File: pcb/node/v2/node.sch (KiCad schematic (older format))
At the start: 99 parts, among them IC1 Ra-01, J1 Sensor1, J10 Conn_02x03_Odd_Even, J11 USB_A, J12 USART2, J13 USART3, J14 LED_EXT, J15 EXT2, J16 USB_OTG, J2 Sensor2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

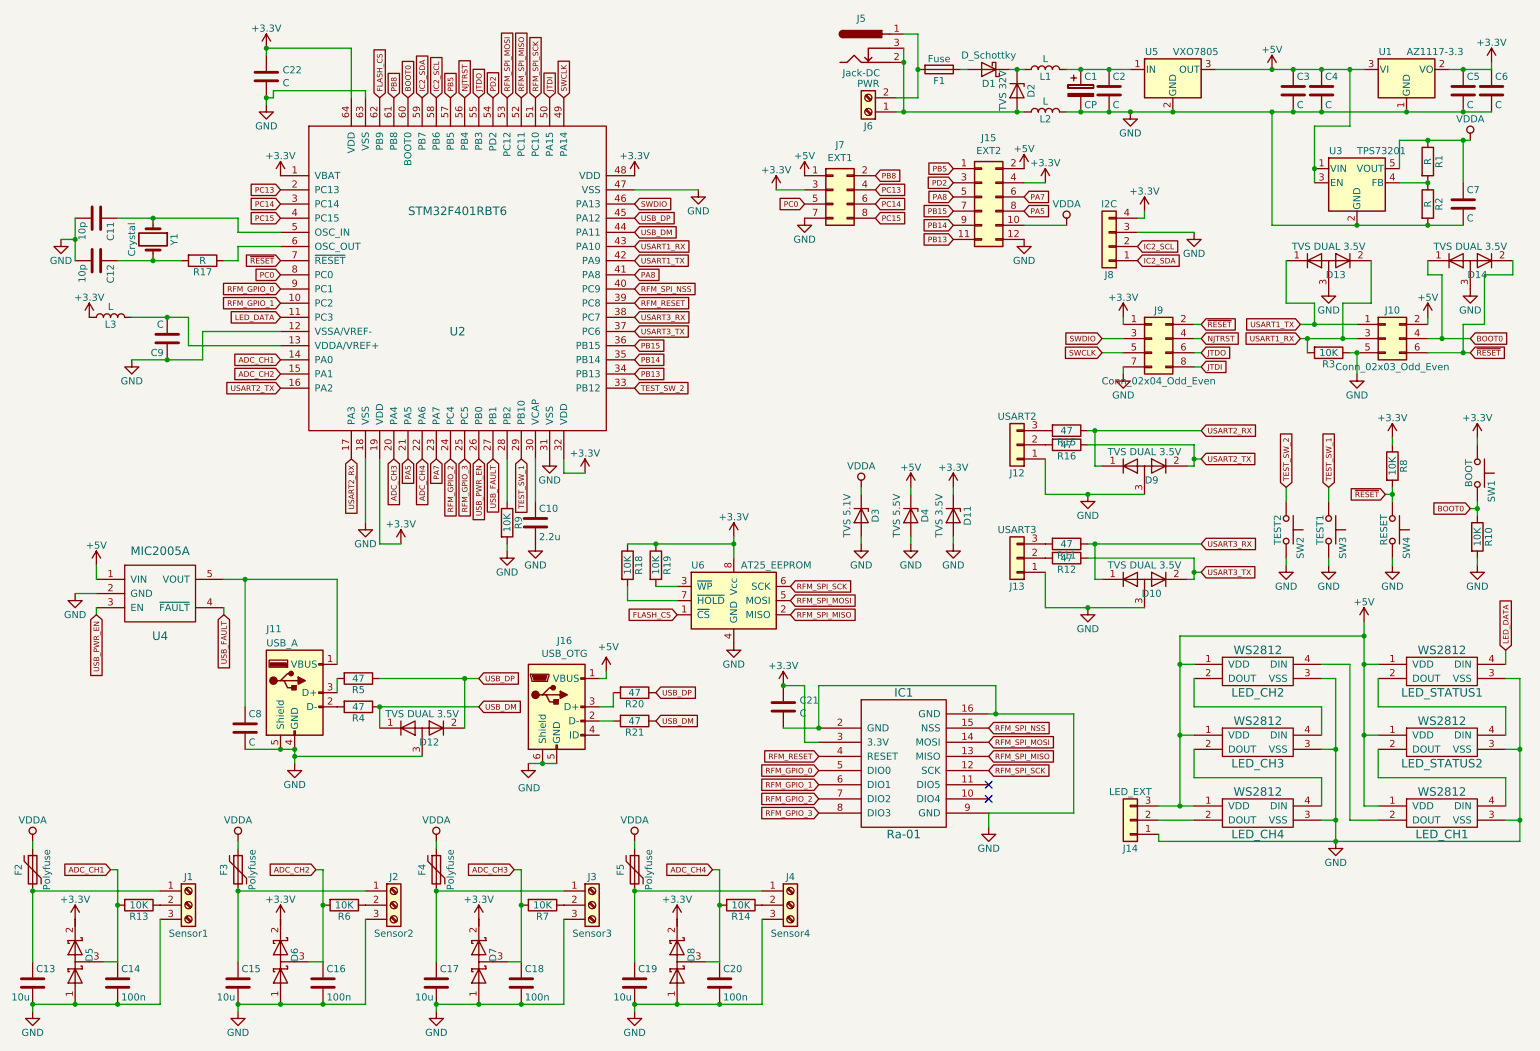
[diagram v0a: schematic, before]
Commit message: Added missing part values
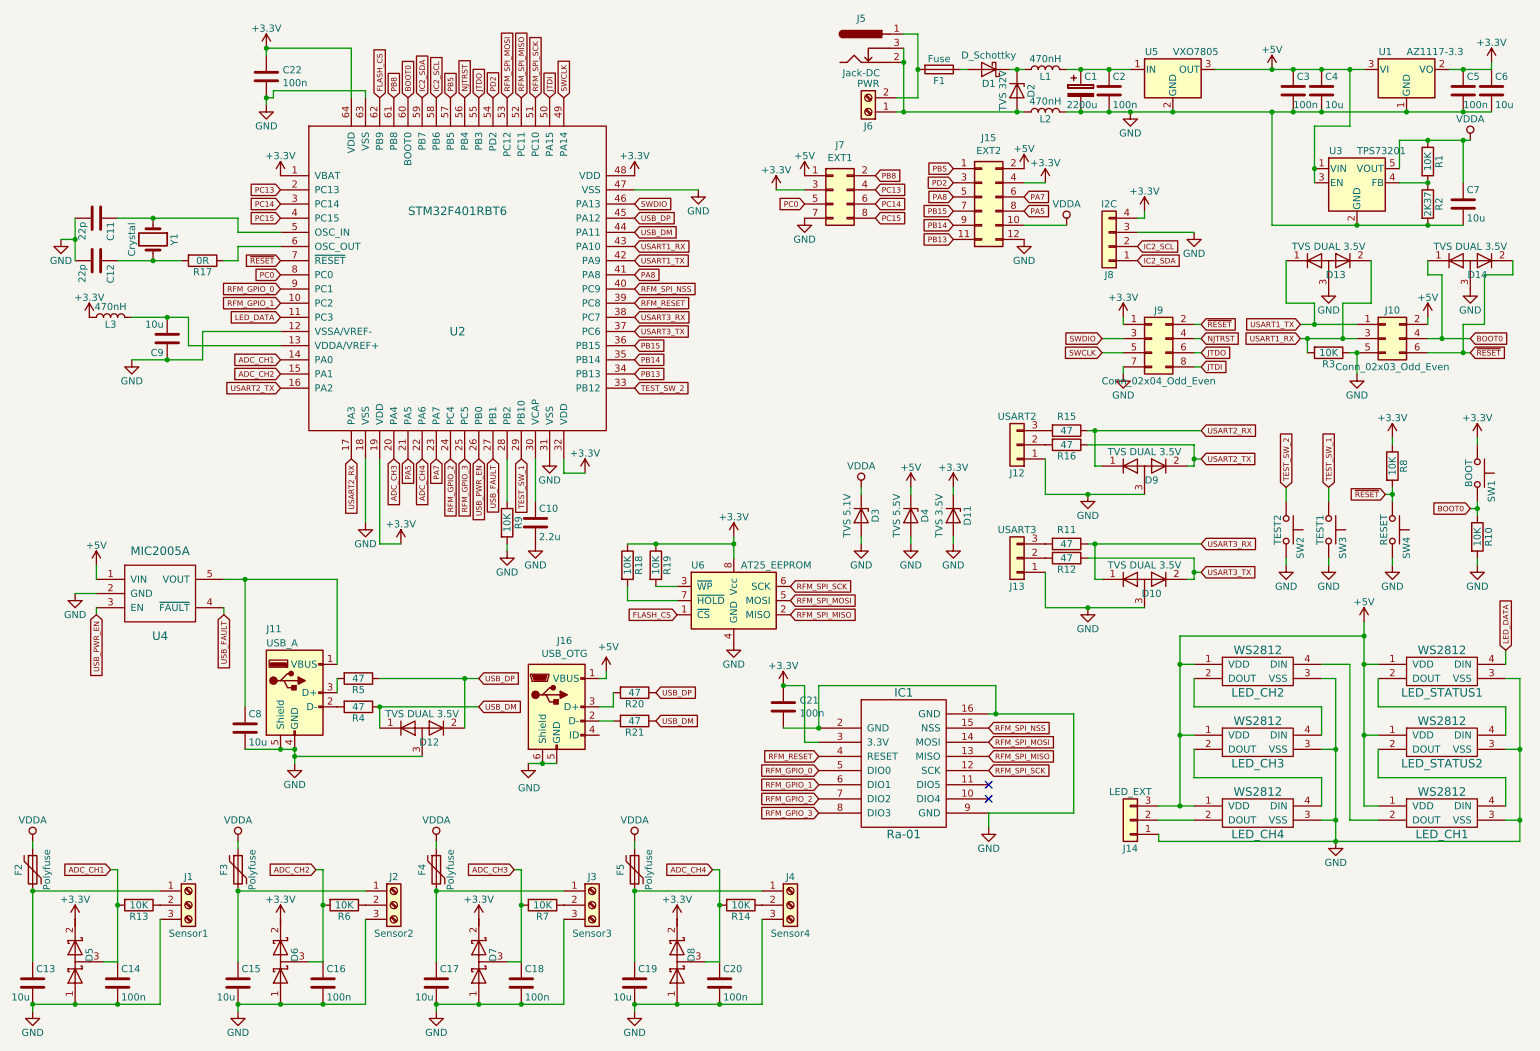
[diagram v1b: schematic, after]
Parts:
- C1: value CP -> 2200u
- C11, C12: value 10p -> 22p
- C2, C21, C22, C3, C5: value C -> 100n
- C4, C6, C7, C8, C9: value C -> 10u
- L1, L2, L3: value L -> 470nH
- R1: value R -> 10K
- R17: value R -> 0R
- R2: value R -> 2K37
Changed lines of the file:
@@
 P 1100 1950
 F 0 "C11" H 1125 2050 50  0000 L CNN
-F 1 "10p" H 1125 1850 50  0000 L CNN
+F 1 "22p" H 1125 1850 50  0000 L CNN
 F 2 "Capacitors_SMD:C_0805" H 1138 1800 50  0001 C CNN
 F 3 "" H 1100 1950 50  0001 C CNN
@@
 P 1100 2250
 F 0 "C12" H 1125 2350 50  0000 L CNN
-F 1 "10p" H 1125 2150 50  0000 L CNN
+F 1 "22p" H 1125 2150 50  0000 L CNN
 F 2 "Capacitors_SMD:C_0805" H 1138 2100 50  0001 C CNN
 F 3 "" H 1100 2250 50  0001 C CNN
@@
 P 10750 1850
 F 0 "C7" H 10775 1950 50  0000 L CNN
-F 1 "C" H 10775 1750 50  0000 L CNN
+F 1 "10u" H 10775 1750 50  0000 L CNN
 F 2 "Capacitors_SMD:C_1206" H 10788 1700 50  0001 C CNN
 F 3 "" H 10750 1850 50  0001 C CNN
@@
 P 10500 1550
 F 0 "R1" V 10580 1550 50  0000 C CNN
-F 1 "R" V 10500 1550 50  0000 C CNN
+F 1 "10K" V 10500 1550 50  0000 C CNN
 F 2 "Resistors_SMD:R_0805" V 10430 1550 50  0001 C CNN
 F 3 "" H 10500 1550 50  0001 C CNN
@@
 P 10500 1850
 F 0 "R2" V 10580 1850 50  0000 C CNN
-F 1 "R" V 10500 1850 50  0000 C CNN
+F 1 "2K37" V 10500 1850 50  0000 C CNN
 F 2 "Resistors_SMD:R_0805" V 10430 1850 50  0001 C CNN
 F 3 "" H 10500 1850 50  0001 C CNN
@@
 P 1600 2800
 F 0 "C9" H 1625 2900 50  0000 L CNN
-F 1 "C" H 1625 2700 50  0000 L CNN
+F 1 "10u" H 1625 2700 50  0000 L CNN
 F 2 "Capacitors_SMD:C_1206" H 1638 2650 50  0001 C CNN
 F 3 "" H 1600 2800 50  0001 C CNN
@@
 P 1200 2650
 F 0 "L3" V 1150 2650 50  0000 C CNN
-F 1 "L" V 1275 2650 50  0000 C CNN
+F 1 "470nH" V 1275 2650 50  0000 C CNN
 F 2 "Choke_SMD:Choke_SMD_1206_Standard" H 1200 2650 50  0001 C CNN
 F 3 "" H 1200 2650 50  0001 C CNN
@@
 P 2150 5550
 F 0 "C8" H 2175 5650 50  0000 L CNN
-F 1 "C" H 2175 5450 50  0000 L CNN
+F 1 "10u" H 2175 5450 50  0000 L CNN
 F 2 "Capacitors_SMD:C_1206" H 2188 5400 50  0001 C CNN
 F 3 "" H 2150 5550 50  0001 C CNN
@@
 P 8050 1050
 F 0 "C1" H 8075 1150 50  0000 L CNN
-F 1 "CP" H 8075 950 50  0000 L CNN
+F 1 "2200u" H 7950 950 50  0000 L CNN
 F 2 "Capacitors_THT:CP_Radial_D10.0mm_P5.00mm" H 8088 900 50  0001 C CNN
 F 3 "" H 8050 1050 50  0001 C CNN
@@
 P 8250 1050
 F 0 "C2" H 8275 1150 50  0000 L CNN
-F 1 "C" H 8275 950 50  0000 L CNN
+F 1 "100n" H 8275 950 50  0000 L CNN
 F 2 "Capacitors_SMD:C_0805" H 8288 900 50  0001 C CNN
 F 3 "" H 8250 1050 50  0001 C CNN
@@
 P 7800 900
 F 0 "L1" V 7750 900 50  0000 C CNN
-F 1 "L" V 7875 900 50  0000 C CNN
+F 1 "470nH" V 7875 900 50  0000 C CNN
 F 2 "Choke_SMD:Choke_SMD_1206_Standard" H 7800 900 50  0001 C CNN
 F 3 "" H 7800 900 50  0001 C CNN
@@
 P 7800 1200
 F 0 "L2" V 7750 1200 50  0000 C CNN
-F 1 "L" V 7875 1200 50  0000 C CNN
+F 1 "470nH" V 7875 1200 50  0000 C CNN
 F 2 "Choke_SMD:Choke_SMD_1206_Standard" H 7800 1200 50  0001 C CNN
 F 3 "" H 7800 1200 50  0001 C CNN
@@
 P 9550 1050
 F 0 "C3" H 9575 1150 50  0000 L CNN
-F 1 "C" H 9575 950 50  0000 L CNN
+F 1 "100n" H 9550 950 50  0000 L CNN
 F 2 "Capacitors_SMD:C_0805" H 9588 900 50  0001 C CNN
 F 3 "" H 9550 1050 50  0001 C CNN
@@
 P 9750 1050
 F 0 "C4" H 9775 1150 50  0000 L CNN
-F 1 "C" H 9775 950 50  0000 L CNN
+F 1 "10u" H 9775 950 50  0000 L CNN
 F 2 "Capacitors_SMD:C_1206" H 9788 900 50  0001 C CNN
 F 3 "" H 9750 1050 50  0001 C CNN
@@
 P 10750 1050
 F 0 "C5" H 10775 1150 50  0000 L CNN
-F 1 "C" H 10775 950 50  0000 L CNN
+F 1 "100n" H 10750 950 50  0000 L CNN
 F 2 "Capacitors_SMD:C_0805" H 10788 900 50  0001 C CNN
 F 3 "" H 10750 1050 50  0001 C CNN
@@
 P 10950 1050
 F 0 "C6" H 10975 1150 50  0000 L CNN
-F 1 "C" H 10975 950 50  0000 L CNN
+F 1 "10u" H 10975 950 50  0000 L CNN
 F 2 "Capacitors_SMD:C_1206" H 10988 900 50  0001 C CNN
 F 3 "" H 10950 1050 50  0001 C CNN
@@
 U 1 1 5B3A7064
 P 7950 4250
-F 0 "R11" V 8030 4250 50  0000 C CNN
+F 0 "R11" V 7850 4250 50  0000 C CNN
 F 1 "47" V 7950 4250 50  0000 C CNN
 F 2 "Resistors_SMD:R_0805" V 7880 4250 50  0001 C CNN
@@
 P 1850 2250
 F 0 "R17" V 1930 2250 50  0000 C CNN
-F 1 "R" V 1850 2250 50  0000 C CNN
+F 1 "0R" V 1850 2250 50  0000 C CNN
 F 2 "Resistors_SMD:R_0805" V 1780 2250 50  0001 C CNN
 F 3 "" H 1850 2250 50  0001 C CNN
@@
 U 1 1 5B4AC564
 P 7950 3450
-F 0 "R15" V 8030 3450 50  0000 C CNN
+F 0 "R15" V 7850 3450 50  0000 C CNN
 F 1 "47" V 7950 3450 50  0000 C CNN
 F 2 "Resistors_SMD:R_0805" V 7880 3450 50  0001 C CNN
@@
 P 5950 5400
 F 0 "C21" H 6065 5446 50  0000 L CNN
-F 1 "C" H 6065 5355 50  0000 L CNN
+F 1 "100n" H 6065 5355 50  0000 L CNN
 F 2 "Capacitors_SMD:C_0805" H 5988 5250 50  0001 C CNN
 F 3 "" H 5950 5400 50  0001 C CNN
@@
 P 2300 950
 F 0 "C22" H 2415 996 50  0000 L CNN
-F 1 "C" H 2415 905 50  0000 L CNN
+F 1 "100n" H 2415 905 50  0000 L CNN
 F 2 "Capacitors_SMD:C_0805" H 2338 800 50  0001 C CNN
 F 3 "" H 2300 950 50  0001 C CNN
